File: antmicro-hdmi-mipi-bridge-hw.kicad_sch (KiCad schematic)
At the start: 51 parts

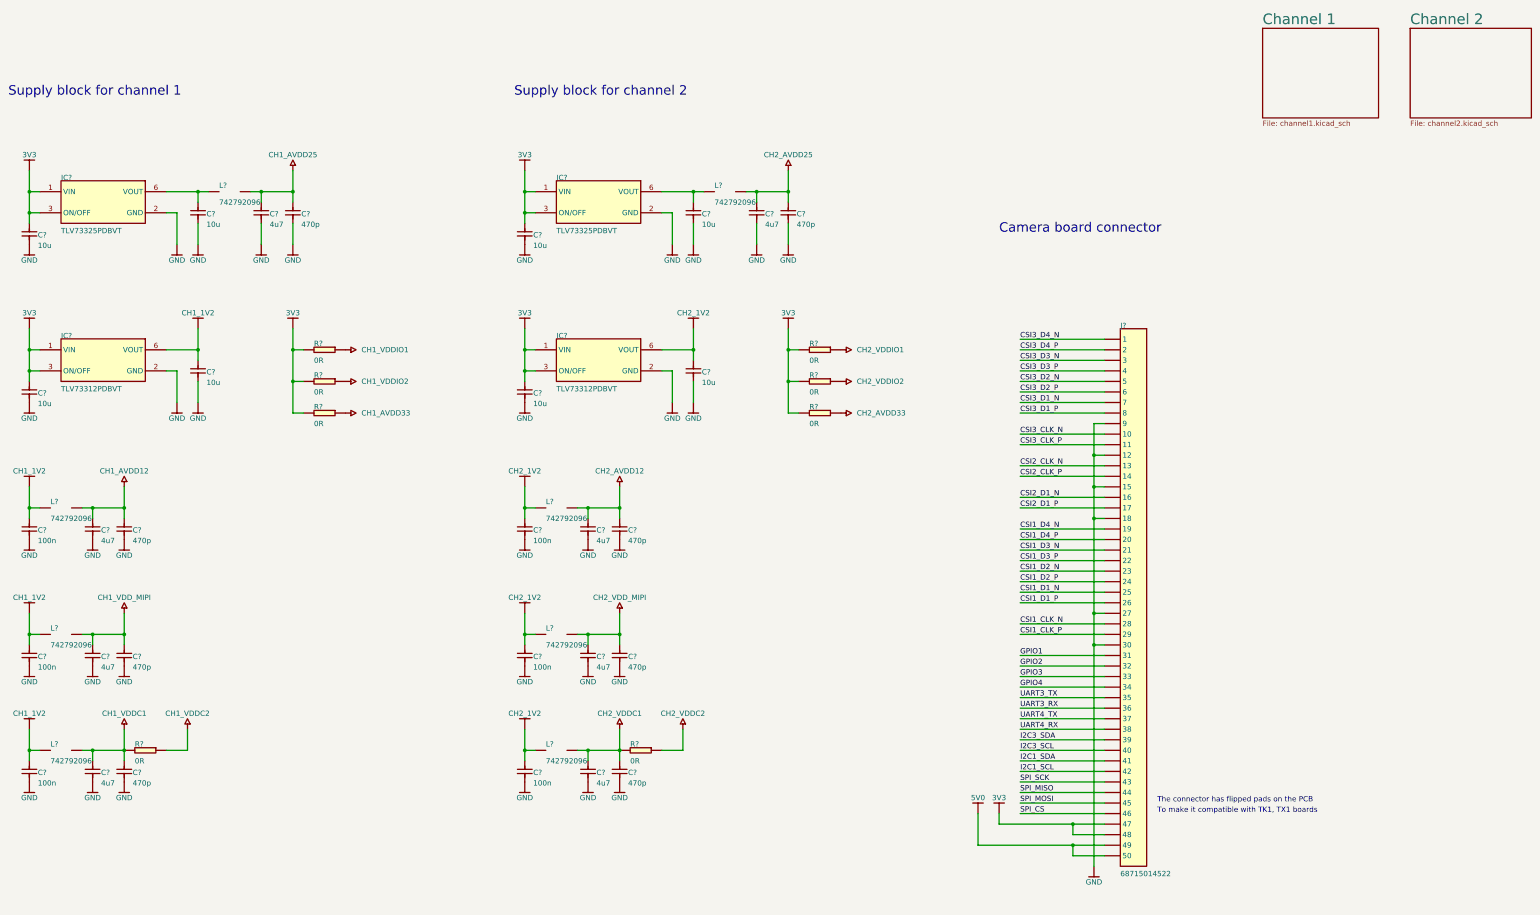
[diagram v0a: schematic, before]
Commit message: Change components to antmicro library ones
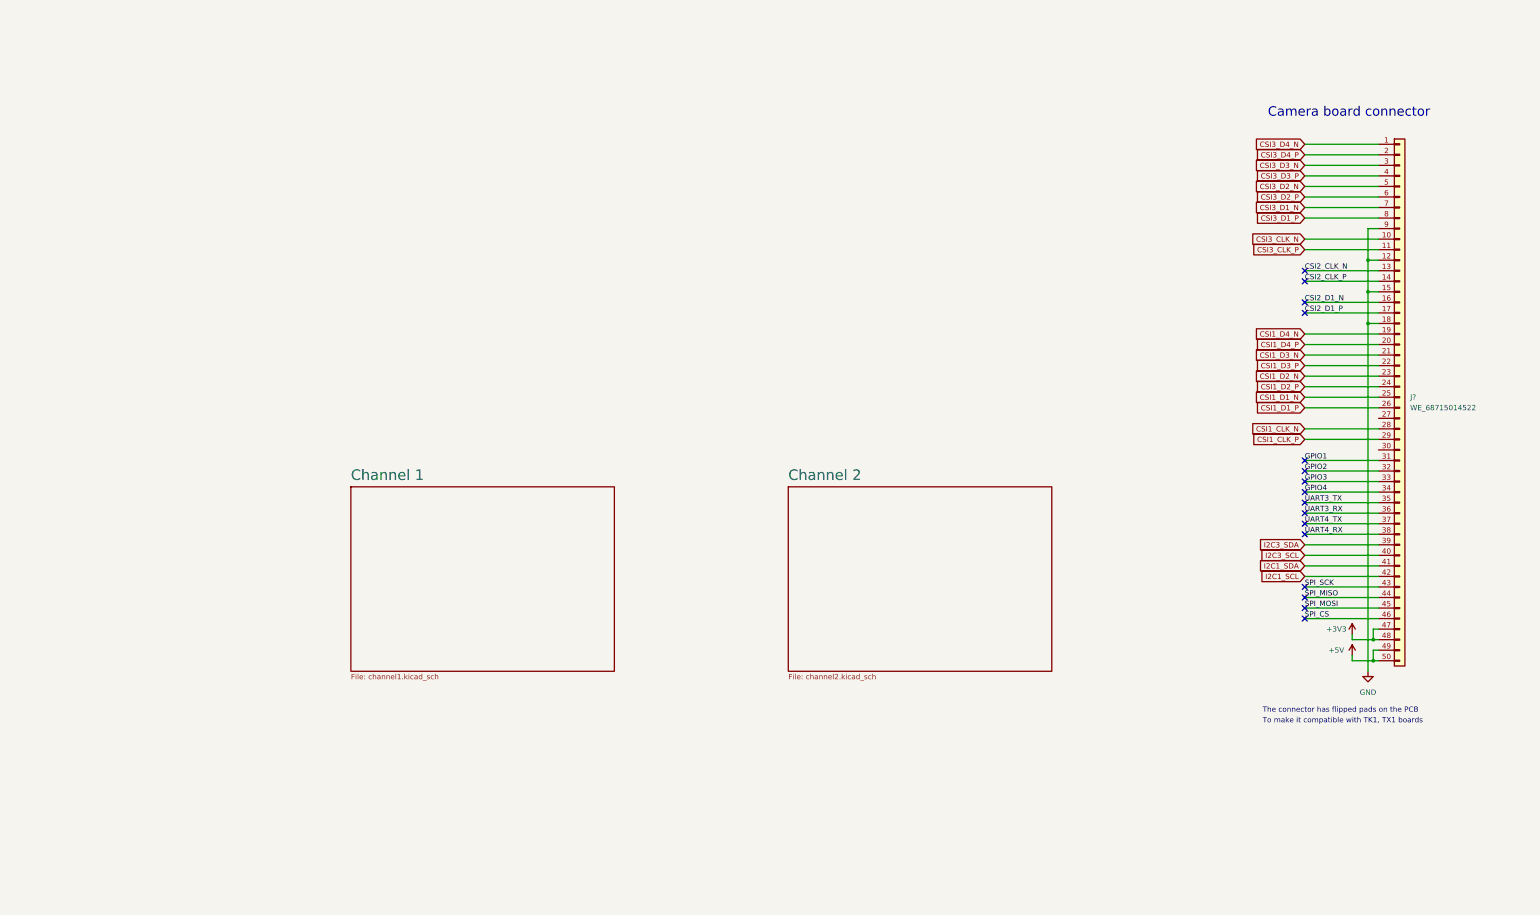
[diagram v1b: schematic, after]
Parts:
- removed C? (x22): ${ALTIUM_VALUE}, HDMI-MIPI-Bridge.Pcblib:0402, symbol altium_import-altium-import:1_C
- removed C? (x8): ${ALTIUM_VALUE}, HDMI-MIPI-Bridge.Pcblib:0603, symbol altium_import-altium-import:1_C
- removed IC? (x4): ${ALTIUM_VALUE}, HDMI-MIPI-Bridge.Pcblib:SOT23-5N, symbol altium_import-altium-import:0_VREG_EN
- removed J?: ${ALTIUM_VALUE}, HDMI-MIPI-Bridge.Pcblib:68715014522_FLIPPED, symbol altium_import-altium-import:0_1X50
- removed L? (x8): ${ALTIUM_VALUE}, HDMI-MIPI-Bridge.Pcblib:0805, symbol altium_import-altium-import:0_Inductor SMT
- removed R? (x8): ${ALTIUM_VALUE}, HDMI-MIPI-Bridge.Pcblib:0603, symbol altium_import-altium-import:0_R
- added J?: WE_68715014522, antmicro-footprints:WE_68715014522, symbol antmicroFCCConnectors:WE_68715014522
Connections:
- net CSI1_CLK_N: now also J?.28 (Pin_28)
- net CSI1_CLK_P: now also J?.29 (Pin_29)
- net CSI1_D1_N: now also J?.25 (Pin_25)
- net CSI1_D1_P: now also J?.26 (Pin_26)
- net CSI1_D2_N: now also J?.23 (Pin_23)
- net CSI1_D2_P: now also J?.24 (Pin_24)
- net CSI1_D3_N: now also J?.21 (Pin_21)
- net CSI1_D3_P: now also J?.22 (Pin_22)
- net CSI1_D4_N: now also J?.19 (Pin_19)
- net CSI1_D4_P: now also J?.20 (Pin_20)
- net CSI2_CLK_N: now also J?.13 (Pin_13)
- net CSI2_CLK_P: now also J?.14 (Pin_14)
- net CSI2_D1_N: now also J?.16 (Pin_16)
- net CSI2_D1_P: now also J?.17 (Pin_17)
- net CSI3_CLK_N: now also J?.10 (Pin_10)
- net CSI3_CLK_P: now also J?.11 (Pin_11)
- net CSI3_D1_N: now also J?.7 (Pin_7)
- net CSI3_D1_P: now also J?.8 (Pin_8)
- net CSI3_D2_N: now also J?.5 (Pin_5)
- net CSI3_D2_P: now also J?.6 (Pin_6)
- net CSI3_D3_N: now also J?.3 (Pin_3)
- net CSI3_D3_P: now also J?.4 (Pin_4)
- net CSI3_D4_N: now also J?.1 (Pin_1)
- net CSI3_D4_P: now also J?.2 (Pin_2)
- net GND: now also J?.12 (Pin_12), J?.15 (Pin_15), J?.18 (Pin_18), J?.9 (Pin_9)
- net GPIO1: now also J?.31 (Pin_31)
- net GPIO2: now also J?.32 (Pin_32)
- net GPIO3: now also J?.33 (Pin_33)
- net GPIO4: now also J?.34 (Pin_34)
- net I2C1_SCL: now also J?.42 (Pin_42)
- net I2C1_SDA: now also J?.41 (Pin_41)
- net I2C3_SCL: now also J?.40 (Pin_40)
- net I2C3_SDA: now also J?.39 (Pin_39)
- net SPI_CS: now also J?.46 (Pin_46)
- net SPI_MISO: now also J?.44 (Pin_44)
- net SPI_MOSI: now also J?.45 (Pin_45)
- net SPI_SCK: now also J?.43 (Pin_43)
- net UART3_RX: now also J?.36 (Pin_36)
- net UART3_TX: now also J?.35 (Pin_35)
- net UART4_RX: now also J?.38 (Pin_38)
- net UART4_TX: now also J?.37 (Pin_37)
- new net +3V3: J?.47 (Pin_47), J?.48 (Pin_48)
- new net +5V: J?.49 (Pin_49), J?.50 (Pin_50)
- no-connect marks 0 -> 16
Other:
- note removed: "Supply block for channel 1"
- note removed: "Supply block for channel 2"

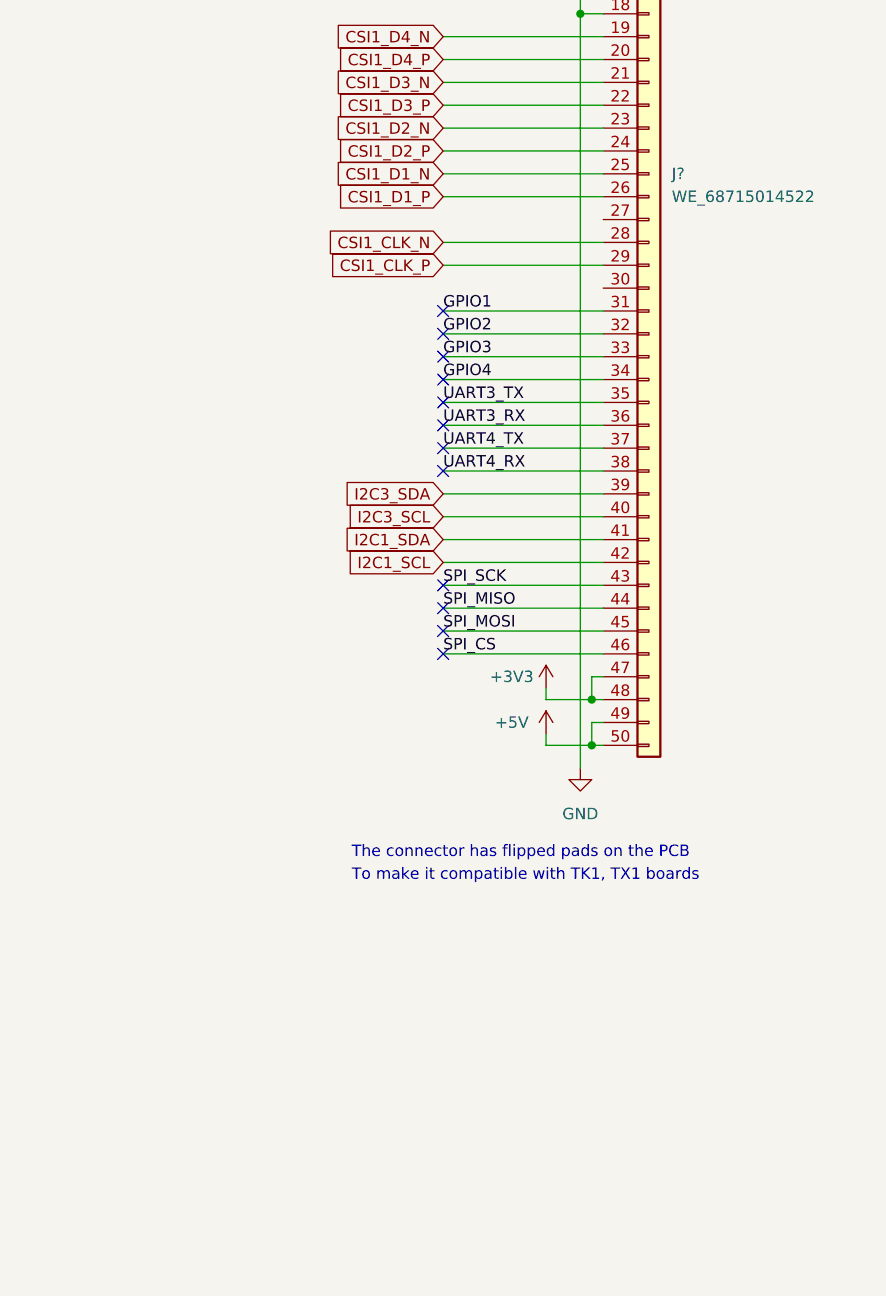
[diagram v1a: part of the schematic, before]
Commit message: Small fixes to decoupling
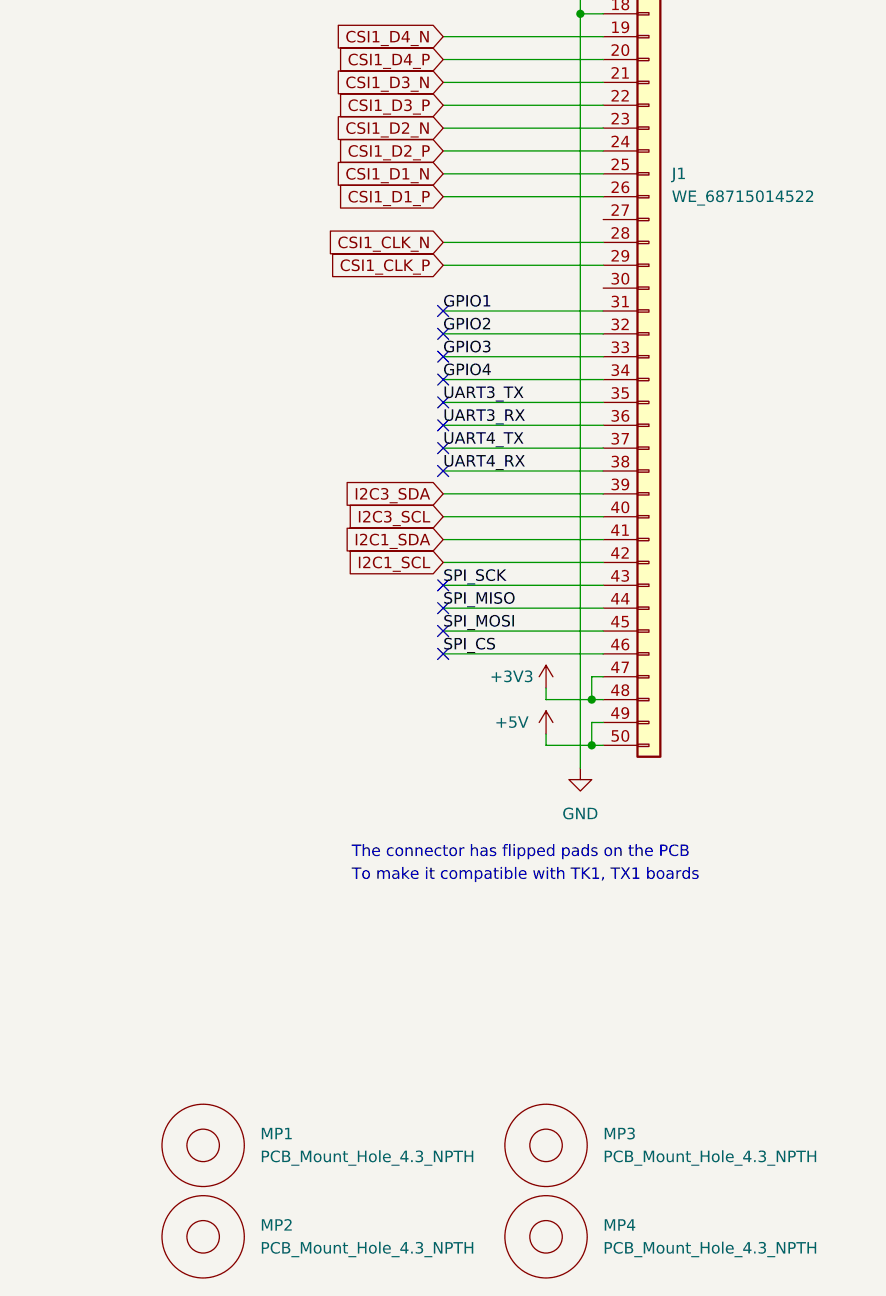
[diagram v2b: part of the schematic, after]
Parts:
- added MP1, MP2, MP3, MP4: PCB_Mount_Hole_4.3_NPTH, antmicro-footprints:mounting-hole-4.2mm-NPTH, symbol antmicroMechanicalParts:PCB_Mount_Hole_4.3_NPTH
- gave numbers to parts that had none: 1
